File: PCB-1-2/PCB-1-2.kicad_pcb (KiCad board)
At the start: 2 copper layers, 76 x 51.5 mm, 44 parts, among them J1 Bus_PCI_Express_x8, J2 ST STDC14 (Debug Connector), J3 USB4105-GF-A, U1 LTC1298IS8_PBF, U10 INA827AIDGKR, U11 LTC1250CS8-PBF, U12 REF3425MDBVTEP, U13 HI-3585APQI, U2 LTC1451IS8-PBF, U3 HI-3110PSIF, U4 FT231XS-R, U5 STM32F103RBT6, U6 STWD100YNXWY3F, U7 ADP7104ACPZ-R7 (v3.3), U8 OPA2187IDGKR, U9 ADP7104ACPZ-R7 (5v), Y1 8MHz Crystal

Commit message: Added used pins to MCU, also semi wired up 429
Still need to look a the devboard schematic for the 429 and use its wiring
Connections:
- J2 pad 08: SWO -> unconnected-(J2-SWO-Pad08)
- J2 pad 13: unconnected-(J2-VCP_RX-Pad13) -> USART1_RX
- J2 pad 14: unconnected-(J2-VCP_TX-Pad14) -> USART1_TX
- J3 pad A4_B9: unconnected-(J3-VBUS-PadA4_B9) -> USB_VDD
- J3 pad A6: unconnected-(J3-DP1-PadA6) -> Net-(J3-DP1)
- J3 pad A7: unconnected-(J3-DN1-PadA7) -> Net-(J3-DN1)
- J3 pad B6: unconnected-(J3-DP2-PadB6) -> Net-(J3-DP1)
- J3 pad B7: unconnected-(J3-DN2-PadB7) -> Net-(J3-DN1)
- U13 pad 15: unconnected-(U13-SCK-Pad15) -> SPI2_SCK
- U13 pad 17: unconnected-(U13-GND-Pad17) -> Transducer-
- U13 pad 19: unconnected-(U13-ACLK-Pad19) -> ARINC_429_CLK
- U13 pad 20: unconnected-(U13-SO-Pad20) -> SPI2_MISO
- U13 pad 3: unconnected-(U13-RINB-Pad3) -> 429_IN-
- U13 pad 30: unconnected-(U13-V_NEG-Pad30) -> -5V
- U13 pad 32: unconnected-(U13-BOUT37-Pad32) -> 429_OUT-
- U13 pad 35: unconnected-(U13-AOUT37-Pad35) -> 429_OUT+
- U13 pad 38: unconnected-(U13-V_POS-Pad38) -> +5V
- U13 pad 40: unconnected-(U13-VDD-Pad40) -> +3.3V
- U13 pad 43: unconnected-(U13-RINA-Pad43) -> 429_IN+
- U13 pad 8: unconnected-(U13-SI-Pad8) -> SPI2_MOSI
- U13 pad 9: unconnected-(U13-~{CS}-Pad9) -> SPI2_CS
- U5 pad 10: unconnected-(U5-PC2-Pad10) -> DISCRETE_OUTPUT_3
- U5 pad 11: unconnected-(U5-PC3-Pad11) -> DISCRETE_OUTPUT_4
- U5 pad 14: unconnected-(U5-PA0-WKUP-Pad14) -> WD_WDI
- U5 pad 15: unconnected-(U5-PA1-Pad15) -> WD_EN
- U5 pad 16: unconnected-(U5-PA2-Pad16) -> USART2_TX
- U5 pad 17: unconnected-(U5-PA3-Pad17) -> USART2_RX
- U5 pad 20: unconnected-(U5-PA4-Pad20) -> SPI1_CS
- U5 pad 21: unconnected-(U5-PA5-Pad21) -> SPI1_SCK
- U5 pad 22: unconnected-(U5-PA6-Pad22) -> SPI1_MISO
- U5 pad 23: unconnected-(U5-PA7-Pad23) -> SPI1_MOSI
- U5 pad 24: unconnected-(U5-PC4-Pad24) -> DISCRETE_OUTPUT_5
- U5 pad 25: unconnected-(U5-PC5-Pad25) -> DISCRETE_OUTPUT_6
- U5 pad 26: unconnected-(U5-PB0-Pad26) -> ARINC_429_CLK
- U5 pad 27: unconnected-(U5-PB1-Pad27) -> HW_ID_1
- U5 pad 28: unconnected-(U5-PB2-Pad28) -> HW_ID_2
- U5 pad 33: SPI2_NSS -> SPI2_CS
- U5 pad 37: unconnected-(U5-PC6-Pad37) -> DISCRETE_INPUT_1
- U5 pad 38: unconnected-(U5-PC7-Pad38) -> DISCRETE_INPUT_2
- U5 pad 39: unconnected-(U5-PC8-Pad39) -> DISCRETE_INPUT_3
- U5 pad 40: unconnected-(U5-PC9-Pad40) -> DISCRETE_INPUT_4
- U5 pad 42: unconnected-(U5-PA9-Pad42) -> USART1_TX
- U5 pad 43: unconnected-(U5-PA10-Pad43) -> USART1_RX
- U5 pad 51: unconnected-(U5-PC10-Pad51) -> DISCRETE_INPUT_5
- U5 pad 52: unconnected-(U5-PC11-Pad52) -> DISCRETE_INPUT_6
- U5 pad 55: unconnected-(U5-PB3-Pad55) -> HW_ID_3
- U5 pad 8: unconnected-(U5-PC0-Pad8) -> DISCRETE_OUTPUT_1
- U5 pad 9: unconnected-(U5-PC1-Pad9) -> DISCRETE_OUTPUT_2

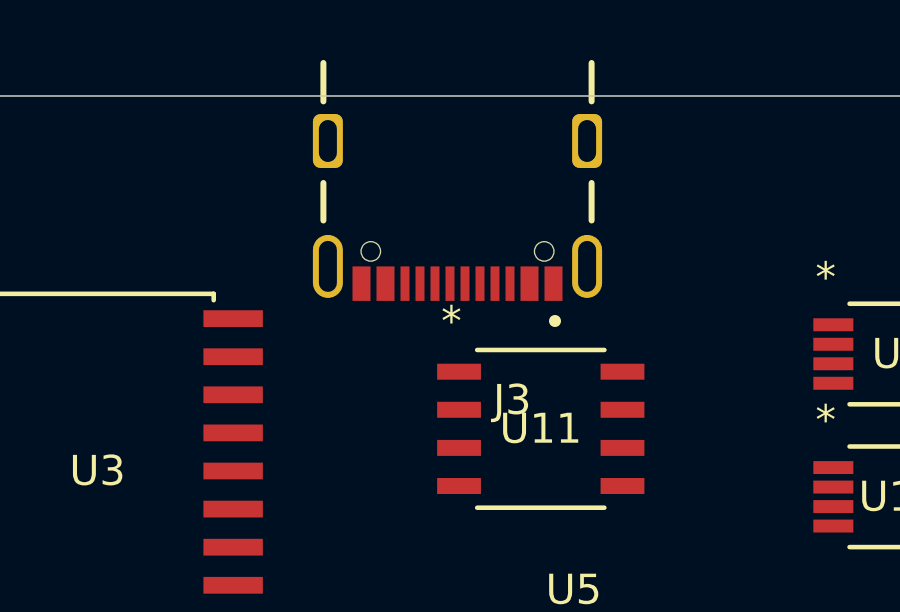
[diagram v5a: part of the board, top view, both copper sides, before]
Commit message: Fixed/Updated the USB-C schematic
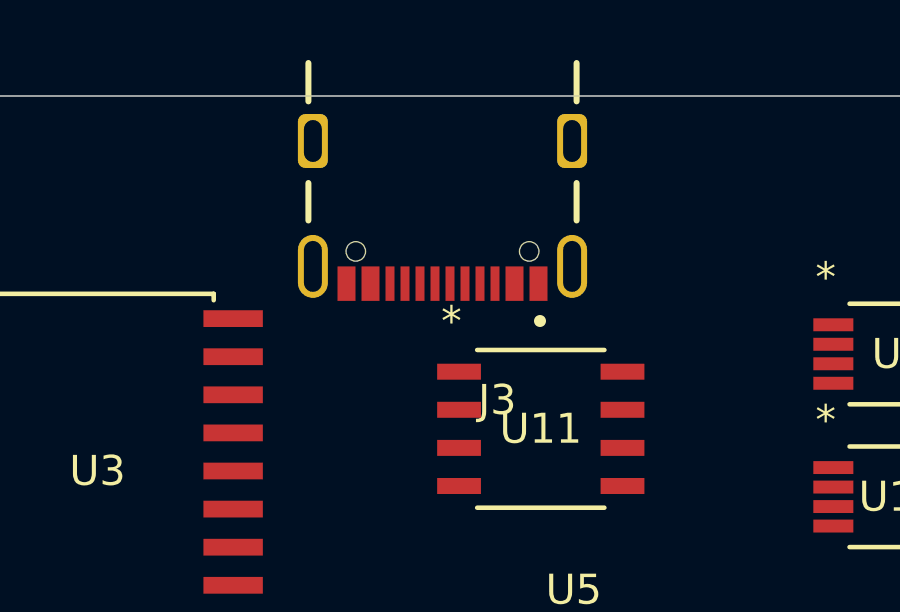
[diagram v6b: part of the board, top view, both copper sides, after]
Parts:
- moved J3 0.50 mm to (40.5, 24.5)
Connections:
- net Net-(J3-DN1) renamed USB_D-
- net Net-(J3-DP1) renamed USB_D+
- J3 pad A1_B12: unconnected-(J3-GND-PadA1_B12) -> Transducer-
- J3 pad A5: unconnected-(J3-CC1-PadA5) -> Net-(J3-CC1)
- J3 pad B1_A12: unconnected-(J3-GND__1-PadB1_A12) -> Transducer-
- J3 pad B4_A9: unconnected-(J3-VBUS__1-PadB4_A9) -> USB_VDD
- J3 pad B5: unconnected-(J3-CC2-PadB5) -> Net-(J3-CC2)
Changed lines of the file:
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@@
 	(net 38 "USART1_TX")
 	(net 39 "USART1_RX")
-	(net 40 "Net-(J3-DN1)")
-	(net 41 "Net-(J3-DP1)")
+	(net 40 "USB_D-")
+	(net 41 "Net-(J3-CC1)")
 	(net 42 "SPI1_MOSI")
 	(net 43 "SPI1_MISO")
@@
 	(net 191 "unconnected-(J3-SHELL_GND-PadSH1)")
 	(net 192 "unconnected-(J3-SHELL_GND__2-PadSH3)")
-	(net 193 "unconnected-(J3-VBUS__1-PadB4_A9)")
-	(net 194 "unconnected-(J3-CC1-PadA5)")
+	(net 193 "USB_D+")
+	(net 194 "Net-(J3-CC2)")
 	(net 195 "unconnected-(J3-SBU2-PadB8)")
-	(net 196 "unconnected-(J3-GND__1-PadB1_A12)")
-	(net 197 "unconnected-(J3-GND-PadA1_B12)")
-	(net 198 "unconnected-(J3-CC2-PadB5)")
-	(net 199 "unconnected-(J3-SHELL_GND__1-PadSH2)")
-	(net 200 "unconnected-(J3-SHELL_GND__3-PadSH4)")
+	(net 196 "unconnected-(J3-SHELL_GND__1-PadSH2)")
+	(net 197 "unconnected-(J3-SHELL_GND__3-PadSH4)")
 	(footprint "Capacitor_SMD:C_0805_2012Metric"
 		(layer "F.Cu")
@@
 	(footprint "SDII LIB:GCT_USB4105-GF-A"
 		(layer "F.Cu")
-		(at 41 24.5 180)
+		(at 40.5 24.5 180)
 		(property "Reference" "J3"
 			(at -1.825 -8.635 180)
@@
 			(size 0.6 1.15)
 			(layers "F.Cu" "F.Paste" "F.Mask")
-			(net 197 "unconnected-(J3-GND-PadA1_B12)")
+			(net 5 "Transducer-")
 			(pinfunction "GND")
 			(pintype "power_in")
@@
 			(size 0.3 1.15)
 			(layers "F.Cu" "F.Paste" "F.Mask")
-			(net 194 "unconnected-(J3-CC1-PadA5)")
+			(net 41 "Net-(J3-CC1)")
 			(pinfunction "CC1")
 			(pintype "bidirectional")
@@
 			(size 0.3 1.15)
 			(layers "F.Cu" "F.Paste" "F.Mask")
-			(net 41 "Net-(J3-DP1)")
+			(net 193 "USB_D+")
 			(pinfunction "DP1")
 			(pintype "bidirectional")
@@
 			(size 0.3 1.15)
 			(layers "F.Cu" "F.Paste" "F.Mask")
-			(net 40 "Net-(J3-DN1)")
+			(net 40 "USB_D-")
 			(pinfunction "DN1")
 			(pintype "bidirectional")
@@
 			(net 190 "unconnected-(J3-SBU1-PadA8)")
 			(pinfunction "SBU1")
-			(pintype "bidirectional")
+			(pintype "bidirectional+no_connect")
 			(solder_mask_margin 0.102)
 		)
@@
 			(size 0.6 1.15)
 			(layers "F.Cu" "F.Paste" "F.Mask")
-			(net 196 "unconnected-(J3-GND__1-PadB1_A12)")
+			(net 5 "Transducer-")
 			(pinfunction "GND__1")
 			(pintype "power_in")
@@
 			(size 0.6 1.15)
 			(layers "F.Cu" "F.Paste" "F.Mask")
-			(net 193 "unconnected-(J3-VBUS__1-PadB4_A9)")
+			(net 7 "USB_VDD")
 			(pinfunction "VBUS__1")
 			(pintype "power_in")
@@
 			(size 0.3 1.15)
 			(layers "F.Cu" "F.Paste" "F.Mask")
-			(net 198 "unconnected-(J3-CC2-PadB5)")
+			(net 194 "Net-(J3-CC2)")
 			(pinfunction "CC2")
 			(pintype "bidirectional")
@@
 			(size 0.3 1.15)
 			(layers "F.Cu" "F.Paste" "F.Mask")
-			(net 41 "Net-(J3-DP1)")
+			(net 193 "USB_D+")
 			(pinfunction "DP2")
 			(pintype "bidirectional")
@@
 			(size 0.3 1.15)
 			(layers "F.Cu" "F.Paste" "F.Mask")
-			(net 40 "Net-(J3-DN1)")
+			(net 40 "USB_D-")
 			(pinfunction "DN2")
 			(pintype "bidirectional")
@@
 			(net 195 "unconnected-(J3-SBU2-PadB8)")
 			(pinfunction "SBU2")
-			(pintype "bidirectional")
+			(pintype "bidirectional+no_connect")
 			(solder_mask_margin 0.102)
 		)
@@
 			(layers "*.Cu" "*.Mask")
 			(remove_unused_layers no)
-			(net 199 "unconnected-(J3-SHELL_GND__1-PadSH2)")
+			(net 196 "unconnected-(J3-SHELL_GND__1-PadSH2)")
 			(pinfunction "SHELL_GND__1")
 			(pintype "power_in")
@@
 			(remove_unused_layers no)
 			(roundrect_rratio 0.25)
-			(net 200 "unconnected-(J3-SHELL_GND__3-PadSH4)")
+			(net 197 "unconnected-(J3-SHELL_GND__3-PadSH4)")
 			(pinfunction "SHELL_GND__3")
 			(pintype "power_in")

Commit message: Updated Schematic & organized the board layout
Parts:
- added C21: 10nF, Capacitor_SMD:C_0805_2012Metric, F.Cu at (204.5, 124.5)
- added C22: 332nF, Capacitor_SMD:C_0805_2012Metric, F.Cu at (212.4, 124.5)
- added C23: 0.015uF, Capacitor_SMD:C_0805_2012Metric, F.Cu at (212.4, 127.5)
- added C24: 0.1uF, Capacitor_SMD:C_0805_2012Metric, F.Cu at (212.4, 130.5)
- added C25: 10nF, Capacitor_SMD:C_0805_2012Metric, F.Cu at (212.4, 133.5)
- added C26: 1uF, Capacitor_SMD:C_0805_2012Metric, F.Cu at (164.1, 136.2)
- added C27: 10uF, Capacitor_SMD:C_0805_2012Metric, F.Cu at (164.1, 139.2)
- added C28: 0.1uF, Capacitor_SMD:C_0805_2012Metric, F.Cu at (157.5, 128.6)
- added C29: 400pF, Capacitor_SMD:C_0805_2012Metric, F.Cu at (168.5, 124.1)
- added C30: 40pF, Capacitor_SMD:C_0805_2012Metric, F.Cu at (168.5, 127.2)
- added C31: 40pF, Capacitor_SMD:C_0805_2012Metric, F.Cu at (168.5, 130.2)
- added C32: 47uF, Capacitor_SMD:C_0805_2012Metric, F.Cu at (105.1, 30.8)
- added C33: 0.1uF, Capacitor_SMD:C_0805_2012Metric, F.Cu at (105.1, 32.8)
- added C34: 0.1uF, Capacitor_SMD:C_0805_2012Metric, F.Cu at (110.5, 32.8)
- added C35: 47uF, Capacitor_SMD:C_0805_2012Metric, F.Cu at (110.5, 30.8)
- added C36: 47uF, Capacitor_SMD:C_0805_2012Metric, F.Cu at (120.5, 42.3)
- added C37: 0.1uF, Capacitor_SMD:C_0805_2012Metric, F.Cu at (120.5, 40.3)
- added C38: 0.1uF, Capacitor_SMD:C_0805_2012Metric, F.Cu at (313.8, 81.2)
- added C39: .001uF, Capacitor_SMD:C_0805_2012Metric, F.Cu at (172.9, 46.6)
- added C40: .01uF, Capacitor_SMD:C_0805_2012Metric, F.Cu at (172.9, 48.9)
- added C41: .1uF, Capacitor_SMD:C_0805_2012Metric, F.Cu at (172.9, 51.1)
- added C42: .1uF, Capacitor_SMD:C_0805_2012Metric, F.Cu at (154.9, 36.5)
- added C43: .01uF, Capacitor_SMD:C_0805_2012Metric, F.Cu at (157.1, 36.5)
- added C44: .001uF, Capacitor_SMD:C_0805_2012Metric, F.Cu at (159.4, 36.5)
- added C45: 10pF, Capacitor_SMD:C_0805_2012Metric, F.Cu at (152.3, 43.3)
- added C46: 10pF, Capacitor_SMD:C_0805_2012Metric, F.Cu at (152.3, 47.3)
- added D1: PWR_LED, LED_SMD:LED_0805_2012Metric, F.Cu at (262.3, 126.2)
- added FB2: 120R, Inductor_SMD:L_0805_2012Metric, F.Cu at (93.2, 103.7)
- added R1: 22, Resistor_SMD:R_0805_2012Metric, F.Cu at (107.8, 54.7)
- added R11: 10k, Resistor_SMD:R_0805_2012Metric, F.Cu at (163.5, 37.5)
- added R12: 1.5Meg, Resistor_SMD:R_0805_2012Metric, F.Cu at (145.0, 44.5)
- added R13: 270, Resistor_SMD:R_0805_2012Metric, F.Cu at (76.6, 54.3)
- added R14: 270, Resistor_SMD:R_0805_2012Metric, F.Cu at (76.6, 57.0)
- added R15: 10.7k, Resistor_SMD:R_0805_2012Metric, F.Cu at (217.4, 125.0)
- added R16: 1.13k, Resistor_SMD:R_0805_2012Metric, F.Cu at (217.4, 128.0)
- added R17: 1M, Resistor_SMD:R_0805_2012Metric, F.Cu at (217.4, 130.9)
- added R18: 1M, Resistor_SMD:R_0805_2012Metric, F.Cu at (217.4, 133.9)
- added R19: 1.13k, Resistor_SMD:R_0805_2012Metric, F.Cu at (221.8, 125.0)
- added R2: 27, Resistor_SMD:R_0805_2012Metric, F.Cu at (65.2, 42.7)
- added R20: 750, Resistor_SMD:R_0805_2012Metric, F.Cu at (221.8, 128.0)
- added R21: 5.5k, Resistor_SMD:R_0805_2012Metric, F.Cu at (169.6, 136.0)
- added R22: 1k, Resistor_SMD:R_0805_2012Metric, F.Cu at (169.6, 139.0)
- added R23: 1k, Resistor_SMD:R_0805_2012Metric, F.Cu at (174.0, 130.1)
- added R24: 2.5k, Resistor_SMD:R_0805_2012Metric, F.Cu at (174.0, 133.1)
- added R25: 5.1k, Resistor_SMD:R_0805_2012Metric, F.Cu at (72.6, 40.3)
- added R26: 5.1k, Resistor_SMD:R_0805_2012Metric, F.Cu at (61.1, 40.3)
- added R27: 4.7k, Resistor_SMD:R_0805_2012Metric, F.Cu at (308.2, 84.2)
- added R28: 2k, Resistor_SMD:R_0805_2012Metric, F.Cu at (262.3, 132.2)
- added R29: 22, Resistor_SMD:R_0805_2012Metric, F.Cu at (210.5, 38.0)
- added R3: 27, Resistor_SMD:R_0805_2012Metric, F.Cu at (68.6, 42.7)
- added R4: 22, Resistor_SMD:R_0805_2012Metric, F.Cu at (207.5, 38.0)
- added Y2: ABM8-24.000MHz-10-B1U-T, SDII LIB:XTAL_ABM8-24.000MHz-10-B1U-T, F.Cu at (148.5, 44.5)
- moved U6 289.1 mm to (313.9, 85.3)
- moved U7 220.9 mm to (264.5, 42.0)
- moved U9 213.0 mm to (265.9, 74.0)
- moved C1 185.8 mm to (218.0, 81.4)
- moved U1 185.8 mm to (211.0, 80.4)
- moved R5 181.3 mm to (265.8, 70.2)
- moved R10 181.2 mm to (264.5, 38.5)
- moved C18 180.8 mm to (261.2, 73.8), turned to -90 degrees
- moved C19 180.3 mm to (260.0, 42.0), turned to -90 degrees
- moved U8 178.7 mm to (204.9, 130.1)
- moved R7 173.7 mm to (258.2, 75.8), turned to 90 degrees
- moved R6 173.6 mm to (258.2, 71.7), turned to 90 degrees
- moved R8 172.7 mm to (257.0, 40.1), turned to 90 degrees
- moved R9 172.6 mm to (257.0, 44.1), turned to 90 degrees
- moved U11 146.5 mm to (161.0, 121.9)
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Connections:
- C1 pad 2: Transducer- -> GND
- C10 pad 1: Transducer- -> GND
- C11 pad 1: Transducer- -> GND
- C12 pad 1: Transducer- -> GND
- C13 pad 2: Transducer- -> GND
- C14 pad 2: Transducer- -> GND
- C15 pad 2: Transducer- -> GND
- C16 pad 2: Transducer- -> GND
- C17 pad 2: Transducer- -> GND
- C18 pad 2: Transducer- -> GND
- C19 pad 2: Transducer- -> GND
- C2 pad 2: Transducer- -> GND
- C20 pad 2: Transducer- -> GND
- C3 pad 2: Transducer- -> GND
- C4 pad 2: Transducer- -> GND
- C5 pad 2: Transducer- -> GND
- C6 pad 1: Transducer- -> GND
- C7 pad 1: Transducer- -> GND
- C8 pad 1: Transducer- -> GND
- C9 pad 1: Transducer- -> GND
- J2 pad 05: Transducer- -> GND
- J2 pad 06: SWCLK -> Net-(J2-SWCLK)
- J2 pad 07: Transducer- -> GND
- J2 pad 11: Transducer- -> GND
- J3 pad A1_B12: Transducer- -> GND
- J3 pad B1_A12: Transducer- -> GND
- J3 pad SH1: unconnected-(J3-SHELL_GND-PadSH1) -> GND
- J3 pad SH2: unconnected-(J3-SHELL_GND__1-PadSH2) -> GND
- J3 pad SH3: unconnected-(J3-SHELL_GND__2-PadSH3) -> GND
- J3 pad SH4: unconnected-(J3-SHELL_GND__3-PadSH4) -> GND
- R7 pad 1: Transducer- -> GND
- R9 pad 1: Transducer- -> GND
- U1 pad 1: SPI2_CS -> SPI1_CS
- U1 pad 4: Transducer- -> GND
- U10 pad 5: Transducer- -> GND
- U10 pad 6: Transducer- -> GND
- U11 pad 4: Transducer- -> GND
- U12 pad 1: Transducer- -> GND
- U12 pad 2: Transducer- -> GND
- U13 pad 17: Transducer- -> Net-(U13-GND)
- U13 pad 25: unconnected-(U13-RFLAG-Pad25) -> 429_RFLAG
- U13 pad 28: unconnected-(U13-TFLAG-Pad28) -> 429_TFLAG
- U13 pad 7: unconnected-(U13-MR-Pad7) -> 429_MR
- U13 pad 9: SPI2_CS -> SPI1_CS
- U2 pad 3: SPI2_CS -> SPI1_CS
- U2 pad 5: Transducer- -> GND
- U3 pad 10: unconnected-(U3-CANH-Pad10) -> 825_CANH
- U3 pad 12: unconnected-(U3-STAT-Pad12) -> 825_STAT
- U3 pad 13: unconnected-(U3-SCK-Pad13) -> SPI1_SCK
- U3 pad 14: unconnected-(U3-SI-Pad14) -> SPI1_MOSI
- U3 pad 15: unconnected-(U3-SO-Pad15) -> SPI1_MISO
- U3 pad 16: unconnected-(U3-*CS-Pad16) -> SPI1_CS
- U3 pad 17: unconnected-(U3-MR-Pad17) -> 825_MR
- U3 pad 18: unconnected-(U3-INT-Pad18) -> 825_INT
- U3 pad 2: unconnected-(U3-OSCOUT-Pad2) -> Net-(U3-OSCOUT)
- U3 pad 3: unconnected-(U3-OSCIN-Pad3) -> Net-(U3-OSCIN)
- U3 pad 4: Net-(D1-A) -> 825_GP1
- U3 pad 5: Net-(D2-A) -> 825_GP2
- U3 pad 6: unconnected-(U3-TXEN-Pad6) -> 825_TXEN
- U3 pad 8: Transducer- -> GND
- U3 pad 9: unconnected-(U3-CANL-Pad9) -> 825_CANL
- U4 pad 16: Transducer- -> GND
- U4 pad 6: Transducer- -> GND
- U5 pad 12: Transducer- -> GND
- U5 pad 18: Transducer- -> GND
- U5 pad 29: unconnected-(U5-PB10-Pad29) -> 429_RFLAG
- U5 pad 30: unconnected-(U5-PB11-Pad30) -> 429_TFLAG
- U5 pad 31: Transducer- -> GND
- U5 pad 33: SPI2_CS -> SPI1_CS
- U5 pad 47: Transducer- -> GND
- U5 pad 53: unconnected-(U5-PC12-Pad53) -> 429_MR
- U5 pad 56: unconnected-(U5-PB4-Pad56) -> 825_INT
- U5 pad 57: unconnected-(U5-PB5-Pad57) -> 825_MR
- U5 pad 58: unconnected-(U5-PB6-Pad58) -> 825_GP1
- U5 pad 59: unconnected-(U5-PB7-Pad59) -> 825_GP2
- U5 pad 60: Transducer- -> GND
- U5 pad 61: unconnected-(U5-PB8-Pad61) -> 825_TXEN
- U5 pad 62: unconnected-(U5-PB9-Pad62) -> 825_STAT
- U5 pad 63: Transducer- -> GND
- U6 pad 1: MCU_NRST -> Net-(U6-*WDO)
- U6 pad 2: Transducer- -> GND
- U7 pad 3: Transducer- -> GND
- U7 pad 6: Transducer- -> GND
- U7 pad 9: Transducer- -> GND
- U8 pad 4: Transducer- -> GND
- U9 pad 3: Transducer- -> GND
- U9 pad 6: Transducer- -> GND
- U9 pad 9: Transducer- -> GND
- Y1 pad 2: Transducer- -> GND
- Y1 pad 4: Transducer- -> GND
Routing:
- net +5V: track 0.00 -> 28.3 mm
- net +3.3V: track 0.00 -> 27.8 mm
- net Net-(U3-OSCIN): track 0.00 -> 20.2 mm
- net Net-(U3-OSCOUT): track 0.00 -> 14.7 mm
- net USB_VDD: track 0.00 -> 14.3 mm, vias 0 -> 2
- net GND: track 0.00 -> 13.0 mm
- net V+_FROM_PCIE: track 0.00 -> 10.6 mm, vias 0 -> 4
- net Net-(U9-PG): track 0.00 -> 8.77 mm
- net Net-(U7-PG): track 0.00 -> 8.71 mm
- net USB_D-: track 0.00 -> 8.04 mm
- net USB_D+: track 0.00 -> 7.98 mm
- net Net-(J3-CC1): track 0.00 -> 5.71 mm
- net Net-(J3-CC2): track 0.00 -> 5.15 mm
- net 825_MR: track 0.00 -> 5.02 mm
- net FT231_3V3OUT: track 0.00 -> 4.85 mm
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
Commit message: Added -5v Inverter
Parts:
- added U14: MAX764ESA, SDII LIB:SO-G8_1_MXM, F.Cu at (298.5, 39.4)
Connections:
- U3 pad 7: unconnected-(U3-SPLIT-Pad7) -> Net-(U3-SPLIT)
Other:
- board size 76 x 51.5 mm -> 89 x 51.5 mm
